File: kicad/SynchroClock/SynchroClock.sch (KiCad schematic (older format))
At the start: 20 parts, among them J1 CLOCK, SW1 FactoryReset, U1 DRV8838, U2 ESP-12E, U3 DS3231, U4 ATMEGA328-PU

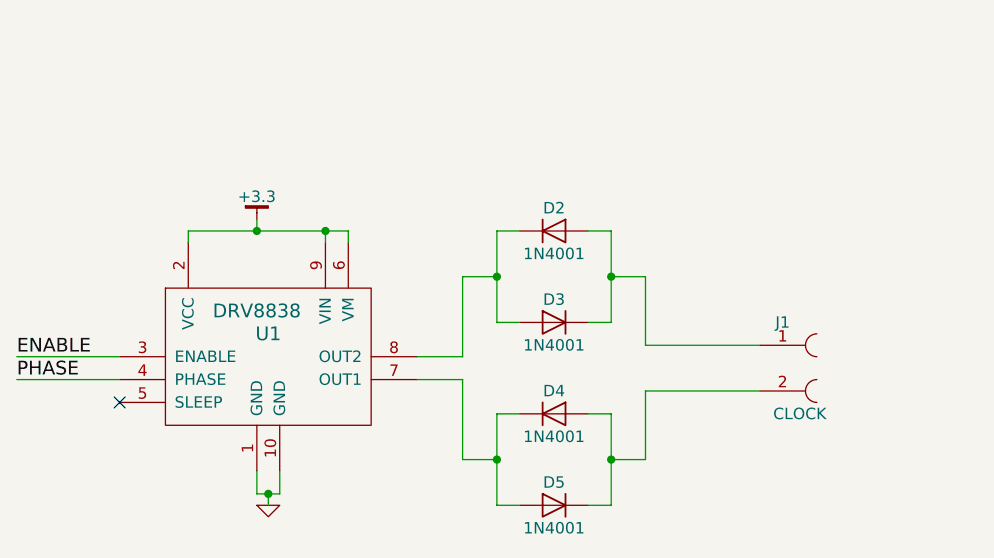
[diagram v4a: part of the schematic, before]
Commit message: use 1.5v to drive clock - better timing 16ms tick pusles and an adjust delay of 8ms
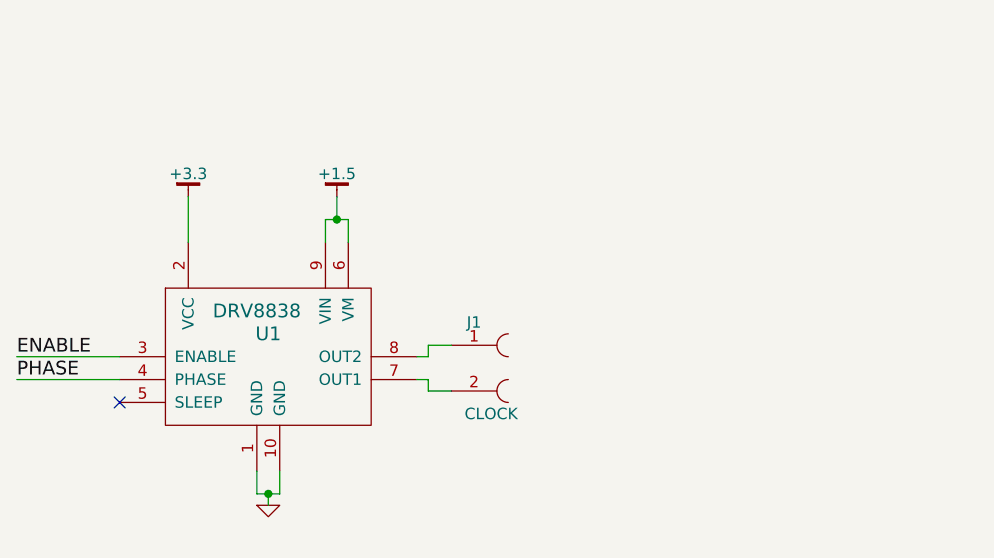
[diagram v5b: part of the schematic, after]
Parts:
- removed D2, D3, D4, D5: 1N4001, Diodes_THT:D_DO-41_SOD81_P2.54mm_Vertical_AnodeUp, symbol 1N4001
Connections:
- net +3.3: no longer U1.6 (VM), U1.9 (VIN)
- net at U1.7 (OUT1): now also J1.2
- net at U1.8 (OUT2): now also J1.1
- new net +1.5: U1.6 (VM), U1.9 (VIN)
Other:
- moved on the sheet: J1
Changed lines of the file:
@@
 L +3.3 #PWR08
 U 1 1 58D7D184
-P 2650 6350
-F 0 "#PWR08" H 2650 6400 30  0001 C CNN
-F 1 "+3.3" H 2650 6450 50  0000 C CNN
-F 2 "" H 2650 6350 60  0000 C CNN
-F 3 "" H 2650 6350 60  0000 C CNN
-	1    2650 6350
-	1    0    0    -1
-$EndComp
-Wire Wire Line
-	2650 6350 2650 6400
-Wire Wire Line
-	2350 6450 2350 6400
-Wire Wire Line
-	2350 6400 3050 6400
-Wire Wire Line
-	2950 6400 2950 6450
-Wire Wire Line
-	3050 6400 3050 6450
-Connection ~ 2650 6400
-Connection ~ 2950 6400
-$Comp
-L 1N4001 D2
-U 1 1 58D7DA00
-P 3950 6400
-F 0 "D2" H 3950 6500 50  0000 C CNN
-F 1 "1N4001" H 3950 6300 50  0000 C CNN
-F 2 "Diodes_THT:D_DO-41_SOD81_P2.54mm_Vertical_AnodeUp" H 3950 6225 50  0001 C CNN
-F 3 "" H 3950 6400 50  0001 C CNN
-	1    3950 6400
-	1    0    0    -1
-$EndComp
-$Comp
-L 1N4001 D3
-U 1 1 58D7DA54
-P 3950 6800
-F 0 "D3" H 3950 6900 50  0000 C CNN
-F 1 "1N4001" H 3950 6700 50  0000 C CNN
-F 2 "Diodes_THT:D_DO-41_SOD81_P2.54mm_Vertical_AnodeUp" H 3950 6625 50  0001 C CNN
-F 3 "" H 3950 6800 50  0001 C CNN
-	1    3950 6800
-	-1   0    0    -1
-$EndComp
-$Comp
-L 1N4001 D4
-U 1 1 58D7DA9D
-P 3950 7200
-F 0 "D4" H 3950 7300 50  0000 C CNN
-F 1 "1N4001" H 3950 7100 50  0000 C CNN
-F 2 "Diodes_THT:D_DO-41_SOD81_P2.54mm_Vertical_AnodeUp" H 3950 7025 50  0001 C CNN
-F 3 "" H 3950 7200 50  0001 C CNN
-	1    3950 7200
-	1    0    0    -1
-$EndComp
-$Comp
-L 1N4001 D5
-U 1 1 58D7DACD
-P 3950 7600
-F 0 "D5" H 3950 7700 50  0000 C CNN
-F 1 "1N4001" H 3950 7500 50  0000 C CNN
-F 2 "Diodes_THT:D_DO-41_SOD81_P2.54mm_Vertical_AnodeUp" H 3950 7425 50  0001 C CNN
-F 3 "" H 3950 7600 50  0001 C CNN
-	1    3950 7600
-	-1   0    0    -1
-$EndComp
-Wire Wire Line
-	4100 7200 4200 7200
-Wire Wire Line
-	4200 7200 4200 7600
-Wire Wire Line
-	4200 7600 4100 7600
-Wire Wire Line
-	3800 7200 3700 7200
-Wire Wire Line
-	3700 7200 3700 7600
-Wire Wire Line
-	3700 7600 3800 7600
-Wire Wire Line
-	3350 7050 3550 7050
-Wire Wire Line
-	3550 7050 3550 7400
-Wire Wire Line
-	3550 7400 3700 7400
-Connection ~ 3700 7400
+P 2350 6250
+F 0 "#PWR08" H 2350 6300 30  0001 C CNN
+F 1 "+3.3" H 2350 6350 50  0000 C CNN
+F 2 "" H 2350 6250 60  0000 C CNN
+F 3 "" H 2350 6250 60  0000 C CNN
+	1    2350 6250
+	1    0    0    -1
+$EndComp
 $Comp
 L CONN_01X02_FEMALE J1
 U 1 1 58D7DDE0
-P 4950 7000
-F 0 "J1" H 4950 7200 50  0000 C CNN
-F 1 "CLOCK" H 5025 6800 50  0000 C CNN
-F 2 "Connectors:PINHEAD1-2" H 4950 7100 50  0001 C CNN
-F 3 "" H 4950 7100 50  0001 C CNN
-	1    4950 7000
-	1    0    0    -1
-$EndComp
-Wire Wire Line
-	3800 6400 3700 6400
-Wire Wire Line
-	3700 6400 3700 6800
-Wire Wire Line
-	3700 6800 3800 6800
-Wire Wire Line
-	3350 6950 3550 6950
-Wire Wire Line
-	3550 6950 3550 6600
-Wire Wire Line
-	3550 6600 3700 6600
-Connection ~ 3700 6600
-Wire Wire Line
-	4100 6400 4200 6400
-Wire Wire Line
-	4200 6400 4200 6800
-Wire Wire Line
-	4200 6800 4100 6800
-Wire Wire Line
-	4850 6900 4350 6900
-Wire Wire Line
-	4350 6900 4350 6600
-Wire Wire Line
-	4350 6600 4200 6600
-Connection ~ 4200 6600
-Wire Wire Line
-	4850 7100 4350 7100
-Wire Wire Line
-	4350 7100 4350 7400
-Wire Wire Line
-	4350 7400 4200 7400
-Connection ~ 4200 7400
+P 3600 7000
+F 0 "J1" H 3600 7200 50  0000 C CNN
+F 1 "CLOCK" H 3675 6800 50  0000 C CNN
+F 2 "Connectors:PINHEAD1-2" H 3600 7100 50  0001 C CNN
+F 3 "" H 3600 7100 50  0001 C CNN
+	1    3600 7000
+	1    0    0    -1
+$EndComp
 $Comp
 L +3.3 #PWR09
@@
 Wire Wire Line
 	4800 3650 5700 3650
+Wire Wire Line
+	3350 6950 3400 6950
+Wire Wire Line
+	3400 6950 3400 6900
+Wire Wire Line
+	3400 6900 3500 6900
+Wire Wire Line
+	3350 7050 3400 7050
+Wire Wire Line
+	3400 7050 3400 7100
+Wire Wire Line
+	3400 7100 3500 7100
+Wire Wire Line
+	2350 6250 2350 6450
+$Comp
+L +1.5 #PWR?
+U 1 1 58DB155F
+P 3000 6250
+F 0 "#PWR?" H 3000 6300 30  0001 C CNN
+F 1 "+1.5" H 3000 6350 50  0000 C CNN
+F 2 "" H 3000 6250 60  0000 C CNN
+F 3 "" H 3000 6250 60  0000 C CNN
+	1    3000 6250
+	1    0    0    -1
+$EndComp
+Wire Wire Line
+	2950 6450 2950 6350
+Wire Wire Line
+	2950 6350 3050 6350
+Wire Wire Line
+	3050 6350 3050 6450
+Wire Wire Line
+	3000 6250 3000 6350
+Connection ~ 3000 6350
 $EndSCHEMATC

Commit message: v1 PCB layout
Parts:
- removed U3: DS3231, Housings_SOIC:SOIC-16_7.5x10.3mm_Pitch1.27mm, symbol DS3231
- added C1: 100nf, Capacitors_THT:C_Disc_D4.3mm_W1.9mm_P5.00mm, symbol C
- added C2: 100uf, Capacitors_THT:CP_Radial_D5.0mm_P2.50mm, symbol CP
- added C3, C4, C5: 0.1uf, Capacitors_THT:C_Disc_D4.3mm_W1.9mm_P5.00mm, symbol C
- added J1: 5v IN, Pin_Headers:Pin_Header_Straight_1x02_Pitch2.54mm, symbol CONN_01X02
- added J2: serial0, Pin_Headers:Pin_Header_Straight_1x06_Pitch2.54mm, symbol CONN_01X06
- added J3: 1.5v battery, Pin_Headers:Pin_Header_Straight_1x02_Pitch2.54mm, symbol CONN_01X02
- added J4: serial1, Pin_Headers:Pin_Header_Straight_1x06_Pitch2.54mm, symbol CONN_01X06
- added J5: ICSP, Pin_Headers:Pin_Header_Straight_2x03_Pitch2.54mm, symbol CONN_02X03
- added M1: DS3231-M, Pin_Headers:Pin_Header_Straight_1x06_Pitch2.54mm, symbol DS3231-M
- added R10: 10k, Resistors_THT:R_Axial_DIN0204_L3.6mm_D1.6mm_P1.90mm_Vertical, symbol R
- added R11: 1k, Resistors_THT:R_Axial_DIN0204_L3.6mm_D1.6mm_P1.90mm_Vertical, symbol R
- added U1: LM1117-3.3, TO_SOT_Packages_THT:TO-220_Vertical, symbol LD1117S33CTR
- added Y1: 8Mhz, Crystals:Resonator_muRata_CSTLSxxxG-3pin_w8.0mm_h3.0mm, symbol Resonator_Small
- J6: renamed from J1; footprint Connectors:PINHEAD1-2 -> Pin_Headers:Pin_Header_Straight_1x02_Pitch2.54mm; symbol CONN_01X02_FEMALE -> CONN_01X02
- U4: renamed from U1; footprint (none) -> Housings_DIP:DIP-10_W7.62mm
- U5: renamed from U4; footprint dip-sip:DIP-28 -> Housings_DIP:DIP-28_W7.62mm
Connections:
- net labels added: MISO, MOSI, RST0, RST1, RX0, RX1, SCK, TX0, TX1
- net labels removed: ENABLE, PHASE, RESET, RX, TX
- wire segments 71 -> 120
- no-connect marks 29 -> 21
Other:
- moved on the sheet: D1, R1, R2, R3, R4, R5, R6, R7, R8, R9, SW1, U2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

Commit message: updated hardware design
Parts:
- removed C2: 100uf, Capacitors_THT:CP_Radial_D5.0mm_P2.50mm, symbol CP
- removed C3: 0.1uf, Capacitors_THT:C_Disc_D4.3mm_W1.9mm_P5.00mm, symbol C
- removed J1: 5v IN, Pin_Headers:Pin_Header_Straight_1x02_Pitch2.54mm, symbol CONN_01X02
- removed J2: serial0, Pin_Headers:Pin_Header_Straight_1x06_Pitch2.54mm, symbol CONN_01X06
- removed J3: 1.5v battery, Pin_Headers:Pin_Header_Straight_1x02_Pitch2.54mm, symbol CONN_01X02
- removed J4: serial1, Pin_Headers:Pin_Header_Straight_1x06_Pitch2.54mm, symbol CONN_01X06
- removed J5: ICSP, Pin_Headers:Pin_Header_Straight_2x03_Pitch2.54mm, symbol CONN_02X03
- removed J6: CLOCK, Pin_Headers:Pin_Header_Straight_1x02_Pitch2.54mm, symbol CONN_01X02
- removed M1: DS3231-M, Pin_Headers:Pin_Header_Straight_1x06_Pitch2.54mm, symbol DS3231-M
- removed U1: LM1117-3.3, TO_SOT_Packages_THT:TO-220_Vertical, symbol LD1117S33CTR
- removed U2: ESP-12E, ESP8266:ESP-12E, symbol ESP-12E
- removed U4: DRV8838, Housings_DIP:DIP-10_W7.62mm, symbol DRV8838
- removed U5: ATMEGA328-PU, Housings_DIP:DIP-28_W7.62mm, symbol ATMEGA328-PU
- removed Y1: 8Mhz, Crystals:Resonator_muRata_CSTLSxxxG-3pin_w8.0mm_h3.0mm, symbol Resonator_Small
- added BT1: 4xAA, Pin_Headers:Pin_Header_Straight_1x02_Pitch2.54mm, symbol Battery
- added BT2: CR2032, Connectors:CR2032V, symbol Battery_Cell
- added C2, C7: 0.1uf, Capacitors_THT:C_Disc_D5.0mm_W2.5mm_P2.50mm, symbol C
- added C3: 100uf, Capacitors_THT:CP_Radial_D6.3mm_P2.50mm, symbol CP
- added J1: SERIAL0, Pin_Headers:Pin_Header_Straight_1x06_Pitch2.54mm, symbol CONN_01X06
- added J4: CLOCK, Pin_Headers:Pin_Header_Straight_1x02_Pitch2.54mm, symbol CONN_01X02
- added R12, R13: 10k, Resistors_THT:R_Axial_DIN0207_L6.3mm_D2.5mm_P2.54mm_Vertical, symbol R
- added U1: TC1262-33VAB, TO_SOT_Packages_THT:TO-220_Vertical, symbol TC1262-33VAB
- added U2: MCP1702-1502E/TO, TO_SOT_Packages_THT:TO-92_Inline_Narrow_Oval, symbol MCP1702-1502E/TO
- added U3: ESP-12E, ESP8266:ESP-12E, symbol ESP-12E
- added U4: DS3231, Housings_SOIC:SOIC-16W_7.5x10.3mm_Pitch1.27mm, symbol DS3231
- added U5: ATTINY85-20PU, Housings_DIP:DIP-8_W7.62mm, symbol ATTINY85-20PU
- added U6: DRV8838, Housings_DIP:DIP-10_W7.62mm, symbol DRV8838
- C1: value 100nf -> 0.1uf; footprint Capacitors_THT:C_Disc_D4.3mm_W1.9mm_P5.00mm -> Capacitors_THT:C_Disc_D5.0mm_W2.5mm_P2.50mm
- C4: value 0.1uf -> 1uf; footprint Capacitors_THT:C_Disc_D4.3mm_W1.9mm_P5.00mm -> Capacitors_THT:C_Disc_D5.0mm_W2.5mm_P2.50mm
- C5: footprint Capacitors_THT:C_Disc_D4.3mm_W1.9mm_P5.00mm -> Capacitors_THT:C_Disc_D5.0mm_W2.5mm_P2.50mm
- R1, R10, R7, R8, R9: footprint Resistors_THT:R_Axial_DIN0204_L3.6mm_D1.6mm_P1.90mm_Vertical -> Resistors_THT:R_Axial_DIN0207_L6.3mm_D2.5mm_P2.54mm_Vertical
- R11, R4: value 1k -> 10k; footprint Resistors_THT:R_Axial_DIN0204_L3.6mm_D1.6mm_P1.90mm_Vertical -> Resistors_THT:R_Axial_DIN0207_L6.3mm_D2.5mm_P2.54mm_Vertical
- R2, R3: value 10k -> 1k; footprint Resistors_THT:R_Axial_DIN0204_L3.6mm_D1.6mm_P1.90mm_Vertical -> Resistors_THT:R_Axial_DIN0207_L6.3mm_D2.5mm_P2.54mm_Vertical
- R5: value 1k -> 220; footprint Resistors_THT:R_Axial_DIN0204_L3.6mm_D1.6mm_P1.90mm_Vertical -> Resistors_THT:R_Axial_DIN0207_L6.3mm_D2.5mm_P2.54mm_Vertical
- R6: value 220 -> 1k; footprint Resistors_THT:R_Axial_DIN0204_L3.6mm_D1.6mm_P1.90mm_Vertical -> Resistors_THT:R_Axial_DIN0207_L6.3mm_D2.5mm_P2.54mm_Vertical
- SW1: value FactoryReset -> SW_Push
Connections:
- net labels added: +1V5, +3V3, GNDREF
- net labels removed: +1.5, +3.3, GND, MISO, MOSI, RST1, RX1, SCK, TX1
- wire segments 120 -> 81
- no-connect marks 21 -> 12

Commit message: added old version new version updated a bit - still not done or compleatly tested
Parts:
- added R14: 10k, Resistors_THT:R_Axial_DIN0207_L6.3mm_D2.5mm_P2.54mm_Vertical, symbol R
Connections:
- net +3V3: now also C2.1, U2.2 (VI), R14.1
- net 1HZ: now also R14.2
- net at BT1.1 (+), C1.1, U1.1 (VIN): no longer C2.1, U2.2 (VI)
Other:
- moved on the sheet: BT1, C2
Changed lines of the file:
@@
 $EndComp
 $Comp
-L GNDREF #PWR20
+L GNDREF #PWR01
 U 1 1 58FCD4F4
 P 9000 6450
-F 0 "#PWR20" H 9000 6200 50  0001 C CNN
+F 0 "#PWR01" H 9000 6200 50  0001 C CNN
 F 1 "GNDREF" H 9000 6300 50  0001 C CNN
 F 2 "" H 9000 6450 50  0001 C CNN
@@
 $EndComp
 $Comp
-L GNDREF #PWR5
+L GNDREF #PWR02
 U 1 1 58FCD4C7
 P 2550 7300
-F 0 "#PWR5" H 2550 7050 50  0001 C CNN
+F 0 "#PWR02" H 2550 7050 50  0001 C CNN
 F 1 "GNDREF" H 2550 7150 50  0001 C CNN
 F 2 "" H 2550 7300 50  0001 C CNN
@@
 $EndComp
 $Comp
-L GNDREF #PWR4
+L GNDREF #PWR03
 U 1 1 58FCD608
 P 2550 6450
-F 0 "#PWR4" H 2550 6200 50  0001 C CNN
+F 0 "#PWR03" H 2550 6200 50  0001 C CNN
 F 1 "GNDREF" H 2550 6300 50  0000 C CNN
 F 2 "" H 2550 6450 50  0001 C CNN
@@
 L Battery BT1
 U 1 1 58FCD6BA
-P 1350 6700
-F 0 "BT1" H 1450 6800 50  0000 L CNN
-F 1 "4xAA" H 1450 6700 50  0000 L CNN
-F 2 "Pin_Headers:Pin_Header_Straight_1x02_Pitch2.54mm" V 1350 6760 50  0001 C CNN
-F 3 "" V 1350 6760 50  0001 C CNN
-	1    1350 6700
+P 1350 6050
+F 0 "BT1" H 1450 6150 50  0000 L CNN
+F 1 "4xAA" H 1450 6050 50  0000 L CNN
+F 2 "Pin_Headers:Pin_Header_Straight_1x02_Pitch2.54mm" V 1350 6110 50  0001 C CNN
+F 3 "" V 1350 6110 50  0001 C CNN
+	1    1350 6050
 	0    1    1    0
 $EndComp
@@
 L C C2
 U 1 1 58FCD798
-P 2050 7150
-F 0 "C2" H 2075 7250 50  0000 L CNN
-F 1 "0.1uf" H 2075 7050 50  0000 L CNN
-F 2 "Capacitors_THT:C_Disc_D5.0mm_W2.5mm_P2.50mm" H 2088 7000 50  0001 C CNN
-F 3 "" H 2050 7150 50  0001 C CNN
-	1    2050 7150
+P 1950 7150
+F 0 "C2" H 1975 7250 50  0000 L CNN
+F 1 "0.1uf" H 1975 7050 50  0000 L CNN
+F 2 "Capacitors_THT:C_Disc_D5.0mm_W2.5mm_P2.50mm" H 1988 7000 50  0001 C CNN
+F 3 "" H 1950 7150 50  0001 C CNN
+	1    1950 7150
 	1    0    0    -1
 $EndComp
@@
 $EndComp
 $Comp
-L +1V5 #PWR8
+L +1V5 #PWR04
 U 1 1 58FCDA21
 P 3050 6850
-F 0 "#PWR8" H 3050 6700 50  0001 C CNN
+F 0 "#PWR04" H 3050 6700 50  0001 C CNN
 F 1 "+1V5" H 3050 6990 50  0000 C CNN
 F 2 "" H 3050 6850 50  0001 C CNN
@@
 $EndComp
 $Comp
-L +3V3 #PWR7
+L +3V3 #PWR05
 U 1 1 58FCDA8E
 P 3050 5950
-F 0 "#PWR7" H 3050 5800 50  0001 C CNN
+F 0 "#PWR05" H 3050 5800 50  0001 C CNN
 F 1 "+3V3" H 3050 6090 50  0000 C CNN
 F 2 "" H 3050 5950 50  0001 C CNN
@@
 $EndComp
 $Comp
-L GNDREF #PWR1
+L GNDREF #PWR06
 U 1 1 58FCDB21
-P 1050 6800
-F 0 "#PWR1" H 1050 6550 50  0001 C CNN
-F 1 "GNDREF" H 1050 6650 50  0001 C CNN
-F 2 "" H 1050 6800 50  0001 C CNN
-F 3 "" H 1050 6800 50  0001 C CNN
-	1    1050 6800
-	1    0    0    -1
-$EndComp
-$Comp
-L +3V3 #PWR13
+P 1050 6150
+F 0 "#PWR06" H 1050 5900 50  0001 C CNN
+F 1 "GNDREF" H 1050 6000 50  0001 C CNN
+F 2 "" H 1050 6150 50  0001 C CNN
+F 3 "" H 1050 6150 50  0001 C CNN
+	1    1050 6150
+	1    0    0    -1
+$EndComp
+$Comp
+L +3V3 #PWR07
 U 1 1 58FCE9D2
 P 4950 4700
-F 0 "#PWR13" H 4950 4550 50  0001 C CNN
+F 0 "#PWR07" H 4950 4550 50  0001 C CNN
 F 1 "+3V3" H 4950 4840 50  0000 C CNN
 F 2 "" H 4950 4700 50  0001 C CNN
@@
 $EndComp
 $Comp
-L +3V3 #PWR6
+L +3V3 #PWR08
 U 1 1 58FCEB03
 P 3000 4350
-F 0 "#PWR6" H 3000 4200 50  0001 C CNN
+F 0 "#PWR08" H 3000 4200 50  0001 C CNN
 F 1 "+3V3" H 3000 4490 50  0000 C CNN
 F 2 "" H 3000 4350 50  0001 C CNN
@@
 $EndComp
 $Comp
-L +1V5 #PWR21
+L +1V5 #PWR09
 U 1 1 58FCEBFA
 P 9250 5350
-F 0 "#PWR21" H 9250 5200 50  0001 C CNN
+F 0 "#PWR09" H 9250 5200 50  0001 C CNN
 F 1 "+1V5" H 9250 5490 50  0000 C CNN
 F 2 "" H 9250 5350 50  0001 C CNN
@@
 $EndComp
 $Comp
-L +3V3 #PWR19
+L +3V3 #PWR010
 U 1 1 58FCEC26
 P 8650 5350
-F 0 "#PWR19" H 8650 5200 50  0001 C CNN
+F 0 "#PWR010" H 8650 5200 50  0001 C CNN
 F 1 "+3V3" H 8650 5490 50  0000 C CNN
 F 2 "" H 8650 5350 50  0001 C CNN
@@
 $EndComp
 $Comp
-L GNDREF #PWR15
+L GNDREF #PWR011
 U 1 1 58FCEE96
 P 5700 5900
-F 0 "#PWR15" H 5700 5650 50  0001 C CNN
+F 0 "#PWR011" H 5700 5650 50  0001 C CNN
 F 1 "GNDREF" H 5700 5750 50  0001 C CNN
 F 2 "" H 5700 5900 50  0001 C CNN
@@
 $EndComp
 $Comp
-L GNDREF #PWR18
+L GNDREF #PWR012
 U 1 1 58FCEF51
 P 8650 2850
-F 0 "#PWR18" H 8650 2600 50  0001 C CNN
+F 0 "#PWR012" H 8650 2600 50  0001 C CNN
 F 1 "GNDREF" H 8650 2700 50  0001 C CNN
 F 2 "" H 8650 2850 50  0001 C CNN
@@
 $EndComp
 $Comp
-L +3V3 #PWR17
+L +3V3 #PWR013
 U 1 1 58FCEF83
 P 8050 2850
-F 0 "#PWR17" H 8050 2700 50  0001 C CNN
+F 0 "#PWR013" H 8050 2700 50  0001 C CNN
 F 1 "+3V3" H 8050 2990 50  0000 C CNN
 F 2 "" H 8050 2850 50  0001 C CNN
@@
 $EndComp
 $Comp
-L +3V3 #PWR10
+L +3V3 #PWR014
 U 1 1 58FCF010
 P 3550 2250
-F 0 "#PWR10" H 3550 2100 50  0001 C CNN
+F 0 "#PWR014" H 3550 2100 50  0001 C CNN
 F 1 "+3V3" H 3550 2390 50  0000 C CNN
 F 2 "" H 3550 2250 50  0001 C CNN
@@
 $EndComp
 $Comp
-L GNDREF #PWR11
+L GNDREF #PWR015
 U 1 1 58FCF042
 P 4150 2250
-F 0 "#PWR11" H 4150 2000 50  0001 C CNN
+F 0 "#PWR015" H 4150 2000 50  0001 C CNN
 F 1 "GNDREF" H 4150 2100 50  0001 C CNN
 F 2 "" H 4150 2250 50  0001 C CNN
@@
 1HZ
 $Comp
-L GNDREF #PWR12
+L GNDREF #PWR016
 U 1 1 58FD02C1
 P 4800 3950
-F 0 "#PWR12" H 4800 3700 50  0001 C CNN
+F 0 "#PWR016" H 4800 3700 50  0001 C CNN
 F 1 "GNDREF" H 4800 3800 50  0001 C CNN
 F 2 "" H 4800 3950 50  0001 C CNN
@@
 $EndComp
 $Comp
-L +3V3 #PWR14
+L +3V3 #PWR017
 U 1 1 58FD0E8C
 P 5450 2800
-F 0 "#PWR14" H 5450 2650 50  0001 C CNN
+F 0 "#PWR017" H 5450 2650 50  0001 C CNN
 F 1 "+3V3" H 5450 2940 50  0000 C CNN
 F 2 "" H 5450 2800 50  0001 C CNN
@@
 $EndComp
 $Comp
-L +3V3 #PWR3
+L +3V3 #PWR018
 U 1 1 58FD2620
 P 1750 2450
-F 0 "#PWR3" H 1750 2300 50  0001 C CNN
+F 0 "#PWR018" H 1750 2300 50  0001 C CNN
 F 1 "+3V3" H 1750 2590 50  0000 C CNN
 F 2 "" H 1750 2450 50  0001 C CNN
@@
 $EndComp
 $Comp
-L GNDREF #PWR2
+L GNDREF #PWR019
 U 1 1 58FD2E5E
 P 1200 3450
-F 0 "#PWR2" H 1200 3200 50  0001 C CNN
+F 0 "#PWR019" H 1200 3200 50  0001 C CNN
 F 1 "GNDREF" H 1200 3300 50  0001 C CNN
 F 2 "" H 1200 3450 50  0001 C CNN
@@
 NoConn ~ 3100 1550
 $Comp
-L GNDREF #PWR9
+L GNDREF #PWR020
 U 1 1 58FD3819
 P 3100 1650
-F 0 "#PWR9" H 3100 1400 50  0001 C CNN
+F 0 "#PWR020" H 3100 1400 50  0001 C CNN
 F 1 "GNDREF" H 3100 1500 50  0001 C CNN
 F 2 "" H 3100 1650 50  0001 C CNN
@@
 $EndComp
 $Comp
-L PWR_FLAG #FLG1
+L PWR_FLAG #FLG021
 U 1 1 58FD6A98
-P 1050 6700
-F 0 "#FLG1" H 1050 6775 50  0001 C CNN
-F 1 "PWR_FLAG" H 1050 6850 50  0001 C CNN
-F 2 "" H 1050 6700 50  0001 C CNN
-F 3 "" H 1050 6700 50  0001 C CNN
-	1    1050 6700
-	1    0    0    -1
-$EndComp
-$Comp
-L PWR_FLAG #FLG2
+P 1050 6050
+F 0 "#FLG021" H 1050 6125 50  0001 C CNN
+F 1 "PWR_FLAG" H 1050 6200 50  0001 C CNN
+F 2 "" H 1050 6050 50  0001 C CNN
+F 3 "" H 1050 6050 50  0001 C CNN
+	1    1050 6050
+	1    0    0    -1
+$EndComp
+$Comp
+L PWR_FLAG #FLG022
 U 1 1 58FD6BA1
 P 1550 6050
-F 0 "#FLG2" H 1550 6125 50  0001 C CNN
+F 0 "#FLG022" H 1550 6125 50  0001 C CNN
 F 1 "PWR_FLAG" H 1550 6200 50  0001 C CNN
 F 2 "" H 1550 6050 50  0001 C CNN
@@
 $EndComp
 $Comp
-L PWR_FLAG #FLG3
+L PWR_FLAG #FLG023
 U 1 1 58FD6DCD
 P 6200 5600
-F 0 "#FLG3" H 6200 5675 50  0001 C CNN
+F 0 "#FLG023" H 6200 5675 50  0001 C CNN
 F 1 "PWR_FLAG" H 6200 5750 50  0001 C CNN
 F 2 "" H 6200 5600 50  0001 C CNN
@@
 $EndComp
 $Comp
-L +3V3 #PWR22
+L +3V3 #PWR024
 U 1 1 59054FA0
 P 9850 3200
-F 0 "#PWR22" H 9850 3050 50  0001 C CNN
+F 0 "#PWR024" H 9850 3050 50  0001 C CNN
 F 1 "+3V3" H 9850 3340 50  0000 C CNN
 F 2 "" H 9850 3200 50  0001 C CNN
@@
 $EndComp
 $Comp
-L GNDREF #PWR23
+L GNDREF #PWR025
 U 1 1 59055008
 P 9850 3900
-F 0 "#PWR23" H 9850 3650 50  0001 C CNN
+F 0 "#PWR025" H 9850 3650 50  0001 C CNN
 F 1 "GNDREF" H 9850 3750 50  0001 C CNN
 F 2 "" H 9850 3900 50  0001 C CNN
@@
 	2050 6450 3050 6450
 Wire Wire Line
-	1550 6050 1550 7000
-Wire Wire Line
 	1550 6050 2150 6050
-Connection ~ 1550 6700
+Connection ~ 1550 6050
 Wire Wire Line
 	2050 6150 2050 6050
 Connection ~ 2050 6050
-Wire Wire Line
-	1550 7000 2250 7000
-Connection ~ 2050 7000
-Wire Wire Line
-	2050 7300 3050 7300
 Connection ~ 2550 7300
 Wire Wire Line
@@
 Connection ~ 2550 6450
 Wire Wire Line
-	1150 6700 1050 6700
-Wire Wire Line
-	1050 6700 1050 6800
+	1150 6050 1050 6050
+Wire Wire Line
+	1050 6050 1050 6150
 Wire Wire Line
 	8050 2850 8200 2850
@@
 	5700 4900 5700 4750
 Wire Wire Line
-	5700 4750 4750 4750
+	4750 4750 6200 4750
 Wire Wire Line
 	4750 4750 4750 4800
@@
 $EndComp
 $Comp
-L +3V3 #PWR16
+L +3V3 #PWR026
 U 1 1 59055B8D
 P 7150 4300
-F 0 "#PWR16" H 7150 4150 50  0001 C CNN
+F 0 "#PWR026" H 7150 4150 50  0001 C CNN
 F 1 "+3V3" H 7150 4440 50  0000 C CNN
 F 2 "" H 7150 4300 50  0001 C CNN
@@
 Wire Wire Line
 	7150 4200 7150 4300
+$Comp
+L R R14
+U 1 1 5913D5A0
+P 6200 4950
+F 0 "R14" V 6280 4950 50  0000 C CNN
+F 1 "10k" V 6200 4950 50  0000 C CNN
+F 2 "Resistors_THT:R_Axial_DIN0207_L6.3mm_D2.5mm_P2.54mm_Vertical" V 6130 4950 50  0001 C CNN
+F 3 "" H 6200 4950 50  0001 C CNN
+	1    6200 4950
+	1    0    0    -1
+$EndComp
+Wire Wire Line
+	6200 4750 6200 4800
+Connection ~ 5700 4750
+Wire Wire Line
+	6200 5100 6200 5300
+Connection ~ 6200 5300
+$Comp
+L +3V3 #PWR027
+U 1 1 5913DF42
+P 1950 6850
+F 0 "#PWR027" H 1950 6700 50  0001 C CNN
+F 1 "+3V3" H 1950 6990 50  0000 C CNN
+F 2 "" H 1950 6850 50  0001 C CNN
+F 3 "" H 1950 6850 50  0001 C CNN
+	1    1950 6850
+	1    0    0    -1
+$EndComp
+Wire Wire Line
+	1950 7000 2250 7000
+Wire Wire Line
+	1950 6850 1950 7000
+Wire Wire Line
+	1950 7300 3050 7300
 $EndSCHEMATC
